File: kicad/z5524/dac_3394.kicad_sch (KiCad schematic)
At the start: 46 parts, among them U1 TL074, U14 AD5328, U5 DG442xY

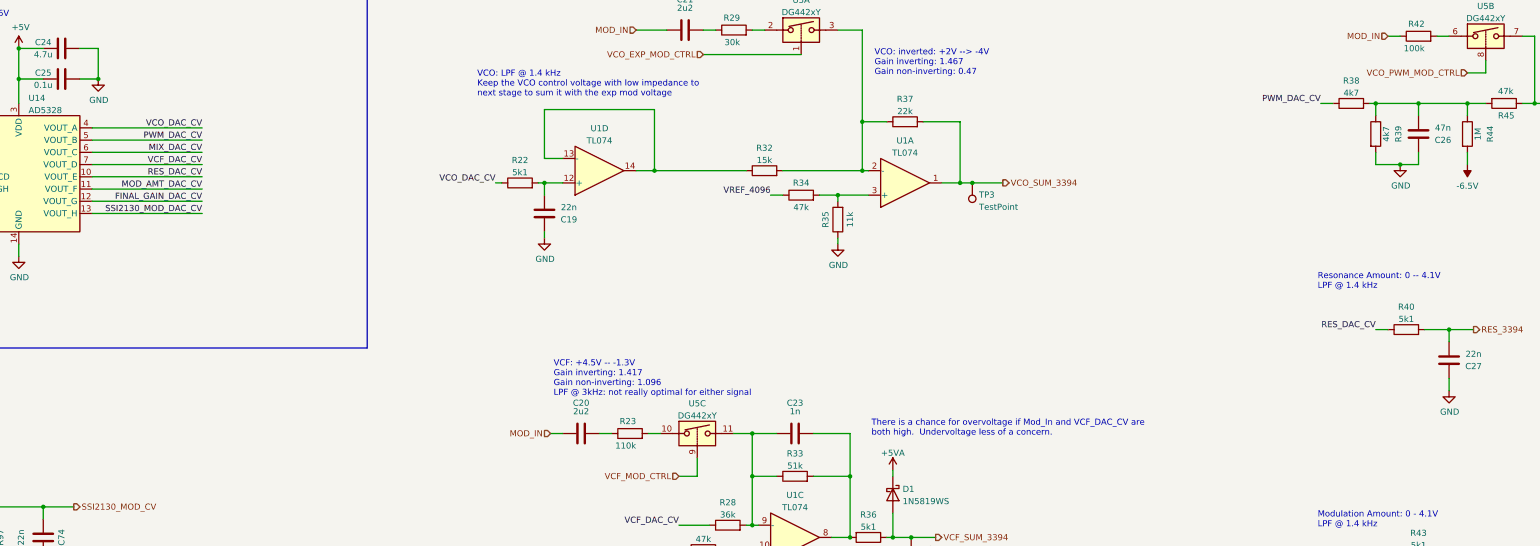
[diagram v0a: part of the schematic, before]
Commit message: move blocks into board for eval
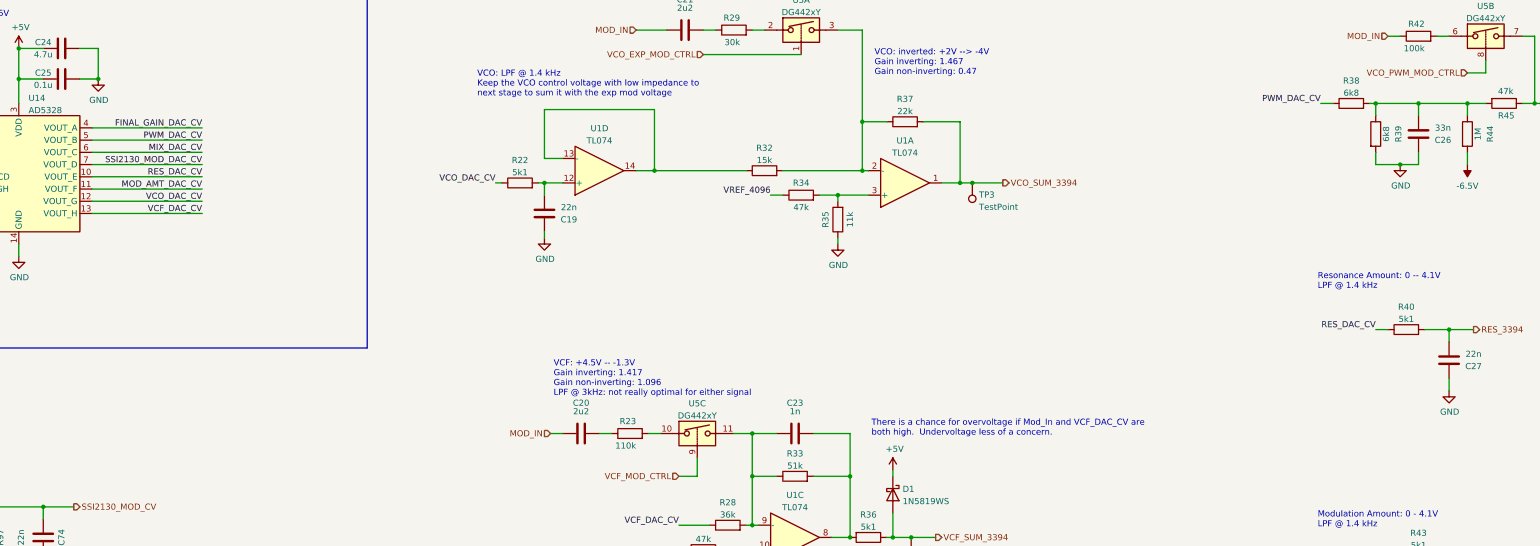
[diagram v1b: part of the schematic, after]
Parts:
- C24: footprint Capacitor_SMD:C_0805_2012Metric -> Capacitor_SMD:C_0603_1608Metric; LCSC Part C1779 -> C19666
- C26: value 47n -> 33n; footprint Capacitor_SMD:C_0805_2012Metric -> Capacitor_SMD:C_0603_1608Metric; LCSC Part C53134 -> C21117
- R38, R39: value 4k7 -> 6k8
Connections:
- net +5VA is gone; now on net +5V: D1.1 (K)
- net FINAL_GAIN_DAC_CV: now also U14.4 (VOUT_A); no longer U14.12 (VOUT_G)
- net SSI2130_MOD_DAC_CV: now also U14.7 (VOUT_D); no longer U14.13 (VOUT_H)
- net VCF_DAC_CV: now also U14.13 (VOUT_H); no longer U14.7 (VOUT_D)
- net VCO_DAC_CV: now also U14.12 (VOUT_G); no longer U14.4 (VOUT_A)
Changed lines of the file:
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@@
     (effects (font (size 1.27 1.27)) (justify right bottom))
   )
-  (label "VCO_DAC_CV" (at 115.57 49.53 180)
-    (effects (font (size 1.27 1.27)) (justify right bottom))
-  )
-  (label "FINAL_GAIN_DAC_CV" (at 115.57 64.77 180)
+  (label "VCO_DAC_CV" (at 115.57 64.77 180)
+    (effects (font (size 1.27 1.27)) (justify right bottom))
+  )
+  (label "FINAL_GAIN_DAC_CV" (at 115.57 49.53 180)
     (effects (font (size 1.27 1.27)) (justify right bottom))
   )
@@
     (effects (font (size 1.27 1.27)) (justify right bottom))
   )
-  (label "SSI2130_MOD_DAC_CV" (at 115.57 67.31 180)
+  (label "SSI2130_MOD_DAC_CV" (at 115.57 57.15 180)
     (effects (font (size 1.27 1.27)) (justify right bottom))
   )
@@
     (effects (font (size 1.27 1.27)) (justify right bottom))
   )
-  (label "VCF_DAC_CV" (at 115.57 57.15 180)
+  (label "VCF_DAC_CV" (at 115.57 67.31 180)
     (effects (font (size 1.27 1.27)) (justify right bottom))
   )
@@
     (in_bom yes) (on_board yes) (fields_autoplaced)
     (property "Reference" "R39" (id 0) (at 364.1258 50.8 90))
-    (property "Value" "4k7" (id 1) (at 361.5889 50.8 90))
+    (property "Value" "6k8" (id 1) (at 361.5889 50.8 90))
     (property "Footprint" "Resistor_SMD:R_0603_1608Metric" (id 2) (at 357.632 50.8 90)
       (effects (font (size 1.27 1.27)) hide)
@@
     (in_bom yes) (on_board yes) (fields_autoplaced)
     (property "Reference" "R38" (id 0) (at 354.33 39.7342 90))
-    (property "Value" "4k7" (id 1) (at 354.33 42.2711 90))
+    (property "Value" "6k8" (id 1) (at 354.33 42.2711 90))
     (property "Footprint" "Resistor_SMD:R_0603_1608Metric" (id 2) (at 354.33 46.228 90)
       (effects (font (size 1.27 1.27)) hide)
@@
     )
     (property "Datasheet" "" (id 3) (at 93.98 39.37 0)
+      (effects (font (size 1.27 1.27)) hide)
+    )
+    (pin "1")
+  )
+  (symbol (lib_id "power:+5V") (at 259.08 120.65 0) (unit 1)
+    (in_bom yes) (on_board yes)
+    (property "Reference" "#PWR043" (id 0) (at 259.08 124.46 0)
+      (effects (font (size 1.27 1.27)) hide)
+    )
+    (property "Value" "+5V" (id 1) (at 259.461 116.2558 0))
+    (property "Footprint" "" (id 2) (at 259.08 120.65 0)
+      (effects (font (size 1.27 1.27)) hide)
+    )
+    (property "Datasheet" "" (id 3) (at 259.08 120.65 0)
       (effects (font (size 1.27 1.27)) hide)
     )
@@
     (property "Reference" "C24" (id 0) (at 82.55 31.75 90))
     (property "Value" "4.7u" (id 1) (at 82.55 34.29 90))
-    (property "Footprint" "Capacitor_SMD:C_0805_2012Metric" (id 2) (at 90.17 32.0548 0)
+    (property "Footprint" "Capacitor_SMD:C_0603_1608Metric" (id 2) (at 90.17 32.0548 0)
       (effects (font (size 1.27 1.27)) hide)
     )
@@
       (effects (font (size 1.27 1.27)) hide)
     )
-    (property "LCSC Part" "C1779" (id 5) (at 86.36 33.02 0)
+    (property "LCSC Part" "C19666" (id 5) (at 86.36 33.02 0)
       (effects (font (size 1.27 1.27)) hide)
     )
@@
     (pin "2")
   )
-  (symbol (lib_id "power:+5VA") (at 259.08 120.65 0) (unit 1)
-    (in_bom yes) (on_board yes) (fields_autoplaced)
-    (property "Reference" "#PWR043" (id 0) (at 259.08 124.46 0)
-      (effects (font (size 1.27 1.27)) hide)
-    )
-    (property "Value" "+5VA" (id 1) (at 259.08 117.0742 0))
-    (property "Footprint" "" (id 2) (at 259.08 120.65 0)
-      (effects (font (size 1.27 1.27)) hide)
-    )
-    (property "Datasheet" "" (id 3) (at 259.08 120.65 0)
-      (effects (font (size 1.27 1.27)) hide)
-    )
-    (pin "1")
-  )
   (symbol (lib_id "Analog_Switch:DG442xY") (at 382.27 30.48 0) (unit 2)
     (in_bom yes) (on_board yes) (fields_autoplaced)
@@
     (in_bom yes) (on_board yes)
     (property "Reference" "C26" (id 0) (at 373.38 52.07 0))
-    (property "Value" "47n" (id 1) (at 373.38 49.53 0))
-    (property "Footprint" "Capacitor_SMD:C_0805_2012Metric" (id 2) (at 369.2652 54.61 0)
+    (property "Value" "33n" (id 1) (at 373.38 49.53 0))
+    (property "Footprint" "Capacitor_SMD:C_0603_1608Metric" (id 2) (at 369.2652 54.61 0)
       (effects (font (size 1.27 1.27)) hide)
     )
@@
       (effects (font (size 1.27 1.27)) hide)
     )
-    (property "LCSC Part" "C53134" (id 4) (at 368.3 50.8 90)
-      (effects (font (size 1.27 1.27)) hide)
-    )
+    (property "LCSC Part" "C21117" (id 4) (at 368.3 50.8 90)
+      (effects (font (size 1.27 1.27)) hide)
+    )

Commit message: tentative power routing
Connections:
- net FINAL_GAIN_DAC_CV: now also U14.6 (VOUT_C); no longer U14.4 (VOUT_A)
- net MIX_DAC_CV: now also U14.4 (VOUT_A); no longer U14.6 (VOUT_C)
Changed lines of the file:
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@@
     (effects (font (size 1.27 1.27)) (justify right bottom))
   )
-  (label "FINAL_GAIN_DAC_CV" (at 115.57 49.53 180)
+  (label "FINAL_GAIN_DAC_CV" (at 115.57 54.61 180)
     (effects (font (size 1.27 1.27)) (justify right bottom))
   )
-  (label "MIX_DAC_CV" (at 115.57 54.61 180)
+  (label "MIX_DAC_CV" (at 115.57 49.53 180)
     (effects (font (size 1.27 1.27)) (justify right bottom))
   )

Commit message: some rather questionable
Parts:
- R24: footprint Resistor_SMD:R_0603_1608Metric -> Resistor_SMD:R_1206_3216Metric
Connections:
- net VREF_4096 is gone; now on net VREF_4.1: R34.1
- net MOD_AMT_DAC_CV: now also U14.7 (VOUT_D); no longer U14.11 (VOUT_F)
- net SSI2130_MOD_DAC_CV: now also U14.11 (VOUT_F); no longer U14.7 (VOUT_D)
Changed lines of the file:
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@@
     (effects (font (size 1.27 1.27)) (justify right bottom))
   )
-  (label "SSI2130_MOD_DAC_CV" (at 115.57 57.15 180)
+  (label "SSI2130_MOD_DAC_CV" (at 115.57 62.23 180)
     (effects (font (size 1.27 1.27)) (justify right bottom))
   )
@@
     (effects (font (size 1.27 1.27)) (justify right bottom))
   )
-  (label "VREF_4096" (at 233.68 63.5 180)
-    (effects (font (size 1.27 1.27)) (justify right bottom))
-  )
   (label "PWM_DAC_CV" (at 115.57 52.07 180)
     (effects (font (size 1.27 1.27)) (justify right bottom))
@@
     (effects (font (size 1.27 1.27)) (justify right bottom))
   )
-  (label "MOD_AMT_DAC_CV" (at 115.57 62.23 180)
+  (label "MOD_AMT_DAC_CV" (at 115.57 57.15 180)
     (effects (font (size 1.27 1.27)) (justify right bottom))
   )
@@
   )
   (hierarchical_label "VREF_4.1" (shape input) (at 214.63 137.16 180)
+    (effects (font (size 1.27 1.27)) (justify right))
+  )
+  (hierarchical_label "VREF_4.1" (shape input) (at 233.68 63.5 180)
     (effects (font (size 1.27 1.27)) (justify right))
   )
@@
     (property "Reference" "R24" (id 0) (at 214.63 203.2 90))
     (property "Value" "10k" (id 1) (at 214.63 198.4811 90))
-    (property "Footprint" "Resistor_SMD:R_0603_1608Metric" (id 2) (at 214.63 202.438 90)
-      (effects (font (size 1.27 1.27)) hide)
-    )
+    (property "Footprint" "Resistor_SMD:R_1206_3216Metric" (id 2) (at 214.63 202.438 90)
+      (effects (font (size 1.27 1.27)) hide)
+    )

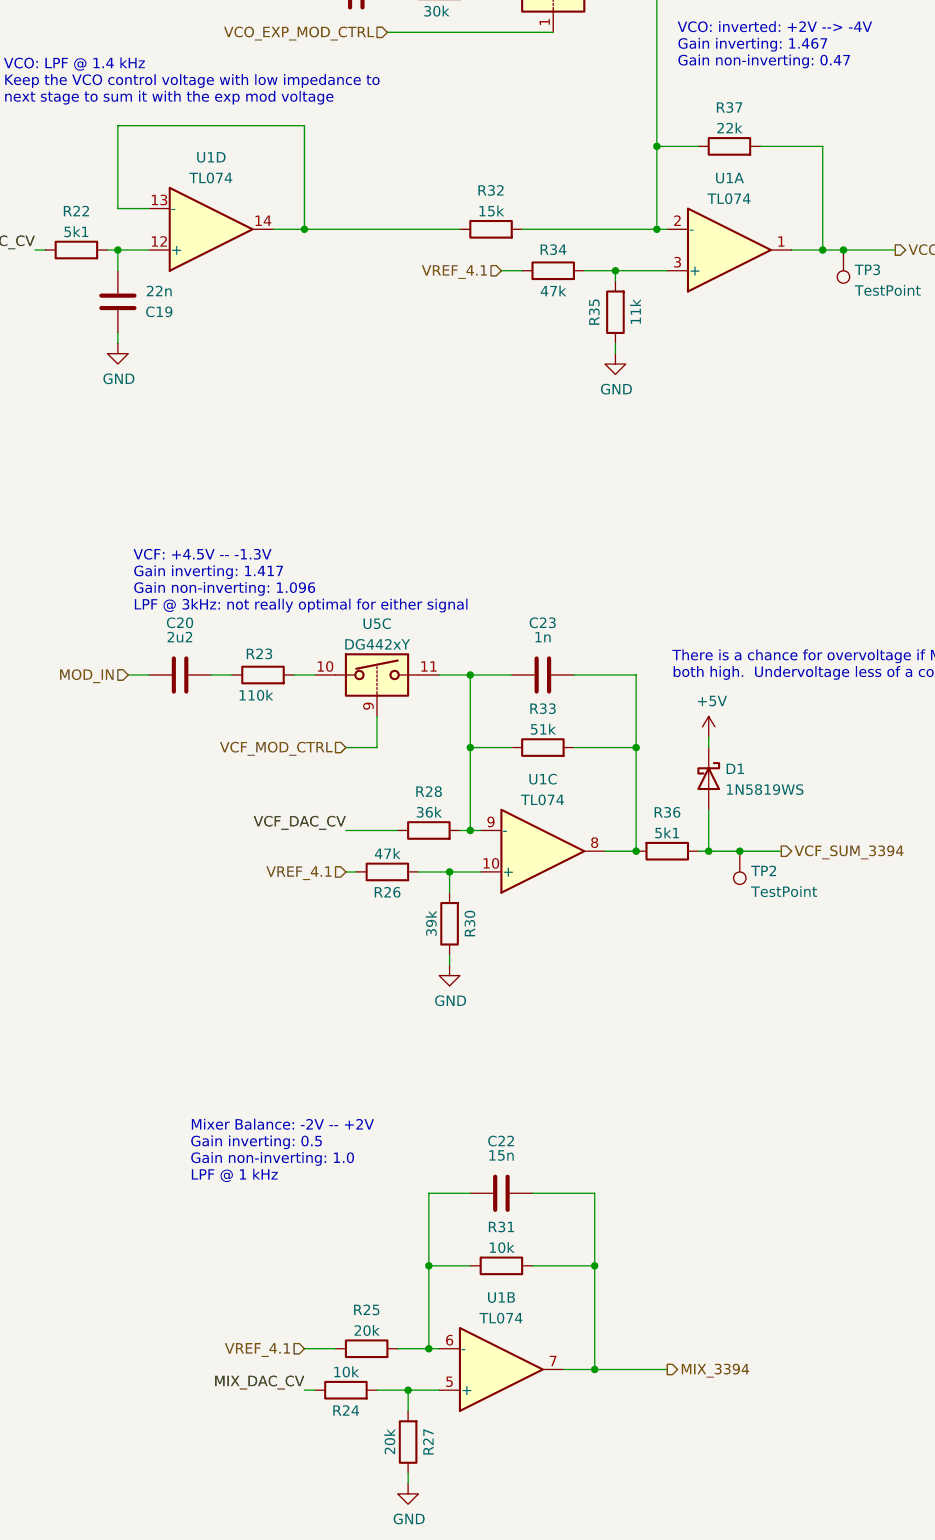
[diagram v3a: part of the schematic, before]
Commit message: non-manhattan routing
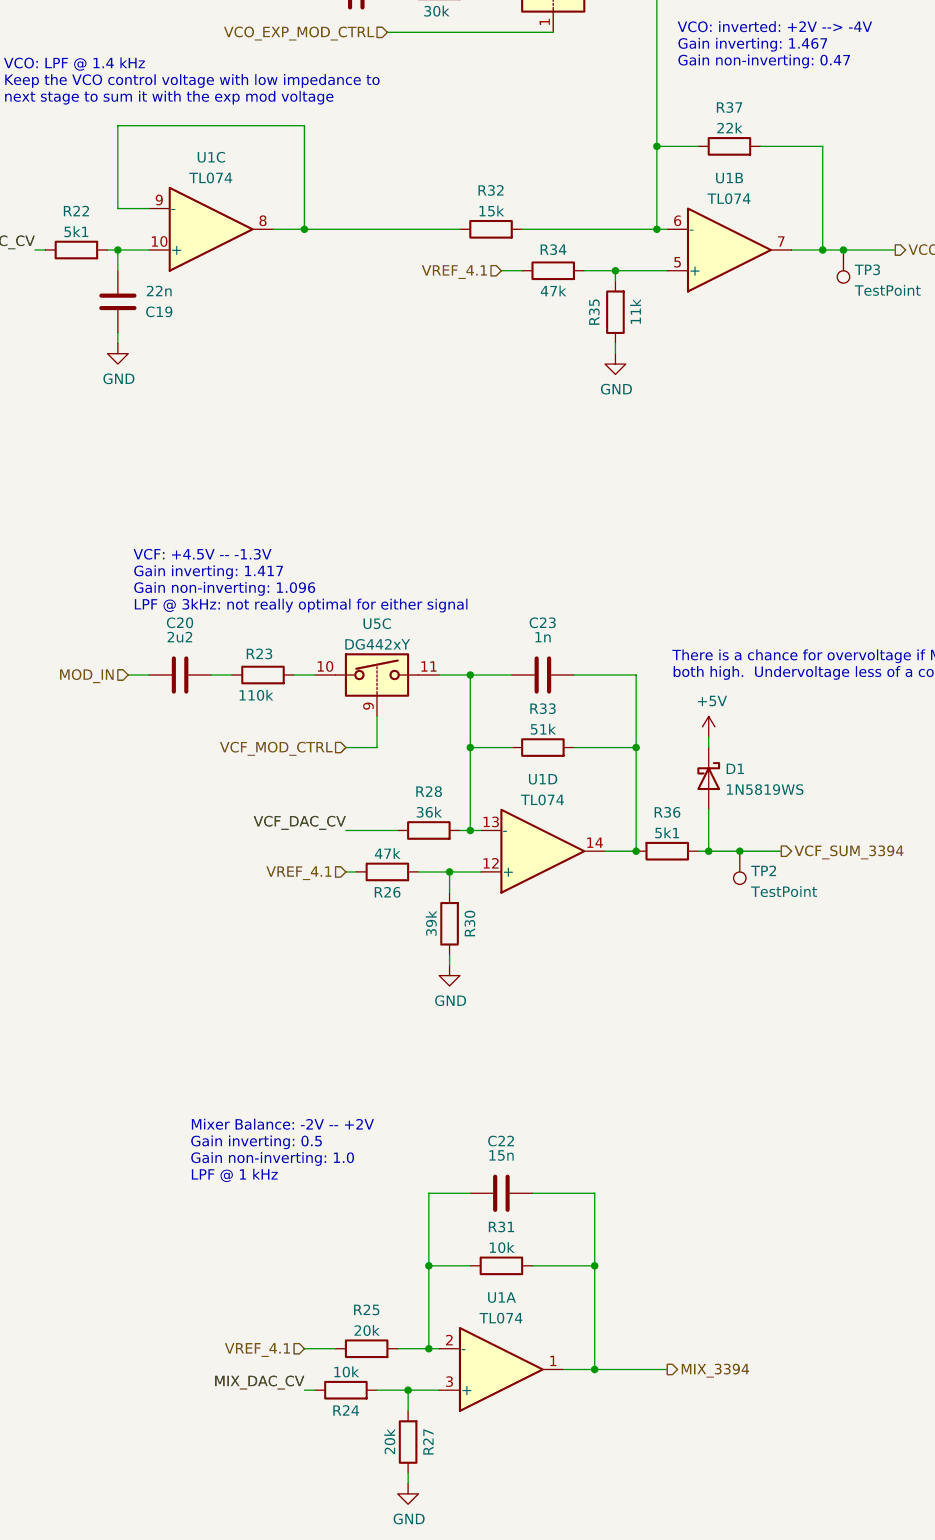
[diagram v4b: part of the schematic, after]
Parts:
- R24: footprint Resistor_SMD:R_1206_3216Metric -> Resistor_SMD:R_0603_1608Metric
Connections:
- net MIX_3394: now also U1.1; no longer U1.7
- net VCO_SUM_3394: now also U1.7; no longer U1.1
- net at R24.2, R27.2: now also U1.3 (+); no longer U1.5 (+)
- net at C22.1, R25.2, R31.1: now also U1.2 (-); no longer U1.6 (-)
- net at C23.1, R28.2, R33.1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: now also U1.13 (-); no longer U1.9 (-)
- net at C23.2, R33.2, R36.2: now also U1.14; no longer U1.8
- net at R34.2, R35.2: now also U1.5 (+); no longer U1.3 (+)
- net at R32.2, R37.1, U5.3: now also U1.6 (-); no longer U1.2 (-)
- net at R26.2, R30.2: now also U1.12 (+); no longer U1.10 (+)
- net at C19.1, R22.2: now also U1.10 (+); no longer U1.12 (+)
- new net: R32.1, U1.8, U1.9 (-)
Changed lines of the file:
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@@
     (pin "2")
   )
-  (symbol (lib_id "Amplifier_Operational:TL074") (at 233.68 198.12 0) (mirror x) (unit 2)
+  (symbol (lib_id "Amplifier_Operational:TL074") (at 233.68 198.12 0) (mirror x) (unit 1)
     (in_bom yes) (on_board yes) (fields_autoplaced)
     (property "Reference" "U1" (id 0) (at 233.68 189.3402 0))
@@
     (property "Reference" "R24" (id 0) (at 214.63 203.2 90))
     (property "Value" "10k" (id 1) (at 214.63 198.4811 90))
-    (property "Footprint" "Resistor_SMD:R_1206_3216Metric" (id 2) (at 214.63 202.438 90)
+    (property "Footprint" "Resistor_SMD:R_0603_1608Metric" (id 2) (at 214.63 202.438 90)
       (effects (font (size 1.27 1.27)) hide)
     )
@@
     (pin "1")
   )
-  (symbol (lib_id "Amplifier_Operational:TL074") (at 198.12 58.42 0) (mirror x) (unit 4)
+  (symbol (lib_id "Amplifier_Operational:TL074") (at 198.12 58.42 0) (mirror x) (unit 3)
     (in_bom yes) (on_board yes) (fields_autoplaced)
     (property "Reference" "U1" (id 0) (at 198.12 49.6402 0))
@@
     (pin "1")
   )
-  (symbol (lib_id "Amplifier_Operational:TL074") (at 261.62 60.96 0) (mirror x) (unit 1)
+  (symbol (lib_id "Amplifier_Operational:TL074") (at 261.62 60.96 0) (mirror x) (unit 2)
     (in_bom yes) (on_board yes) (fields_autoplaced)
     (property "Reference" "U1" (id 0) (at 261.62 52.1802 0))
@@
     (pin "1")
   )
-  (symbol (lib_id "Amplifier_Operational:TL074") (at 238.76 134.62 0) (mirror x) (unit 3)
+  (symbol (lib_id "Amplifier_Operational:TL074") (at 238.76 134.62 0) (mirror x) (unit 4)
     (in_bom yes) (on_board yes) (fields_autoplaced)
     (property "Reference" "U1" (id 0) (at 238.76 125.8402 0))

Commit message: update to kicad 7
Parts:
- renumbered C21 to C29, C20 to C33, C27 to C41, C74 to C44, C28 to C56, C26 to C61, C1 to C63, C23 to C65, C25 to C66, C29 to C67, C22 to C68, C24 to C69, C2 to C71, C19 to C72, D1 to D6, R42 to R32, R29 to R42, R23 to R46, R40 to R54, R97 to R60, R96 to R61, R41 to R62, R45 to R68, R38 to R75, R44 to R76, R39 to R79, R25 to R80, R27 to R81, R32 to R82, R36 to R83, R43 to R84, R34 to R85, R31 to R86, R24 to R87, R33 to R89, R22 to R90, R37 to R91, R35 to R92, R26 to R93, R30 to R95, R28 to R96, TP2 to TP6, TP3 to TP7, U5 to U11, U14 to U17, U1 to U18
